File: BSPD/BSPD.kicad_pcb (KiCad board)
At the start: 2 copper layers, 26 parts, among them J1 440054-2, J2 440054-2, U1 LM339DR, U2 R-78E5.0-0.5, U3 SN74LVC1G08DBVR, U4 SN74LVC3G14DCUR, U5 NE555DR, U6 SN74LVC1G08DBVR, U8 SN74AC32DR

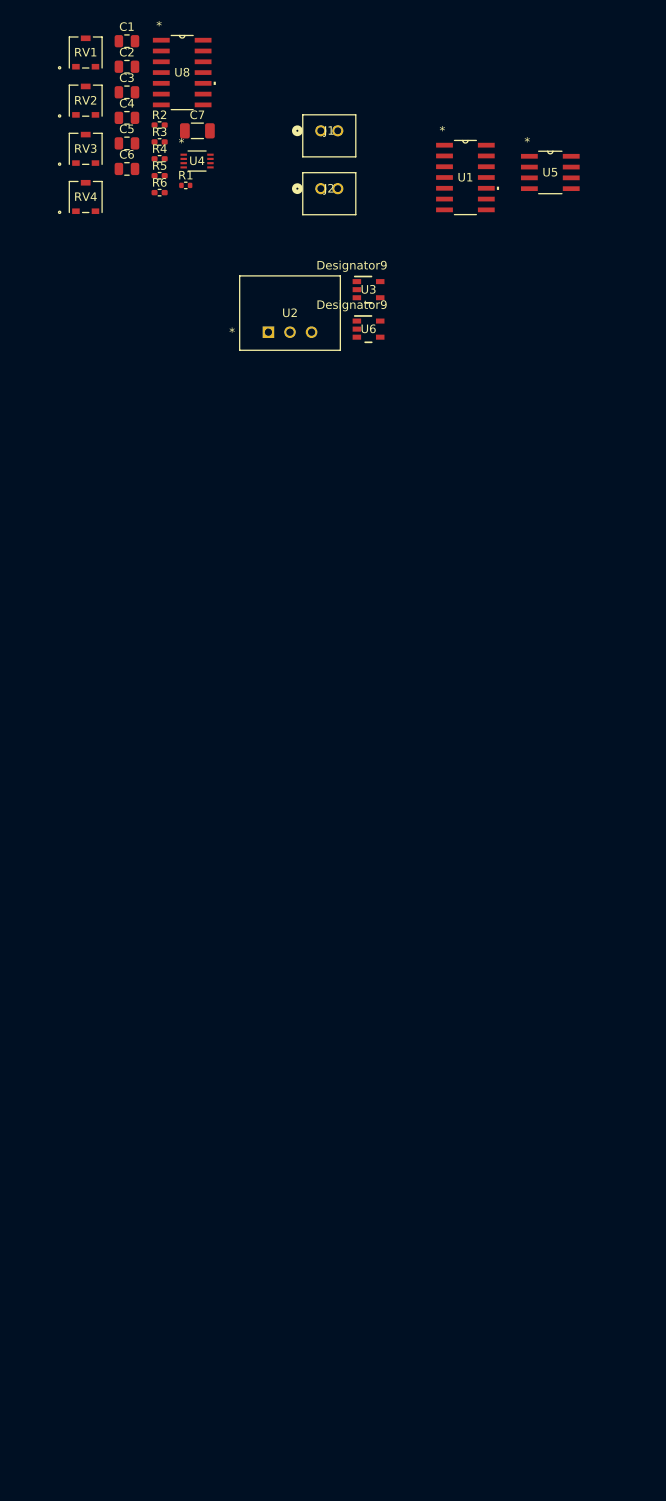
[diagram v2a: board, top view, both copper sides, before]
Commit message: Connector changes, layout, edge cuts, constraints. Need advice on output PMOS
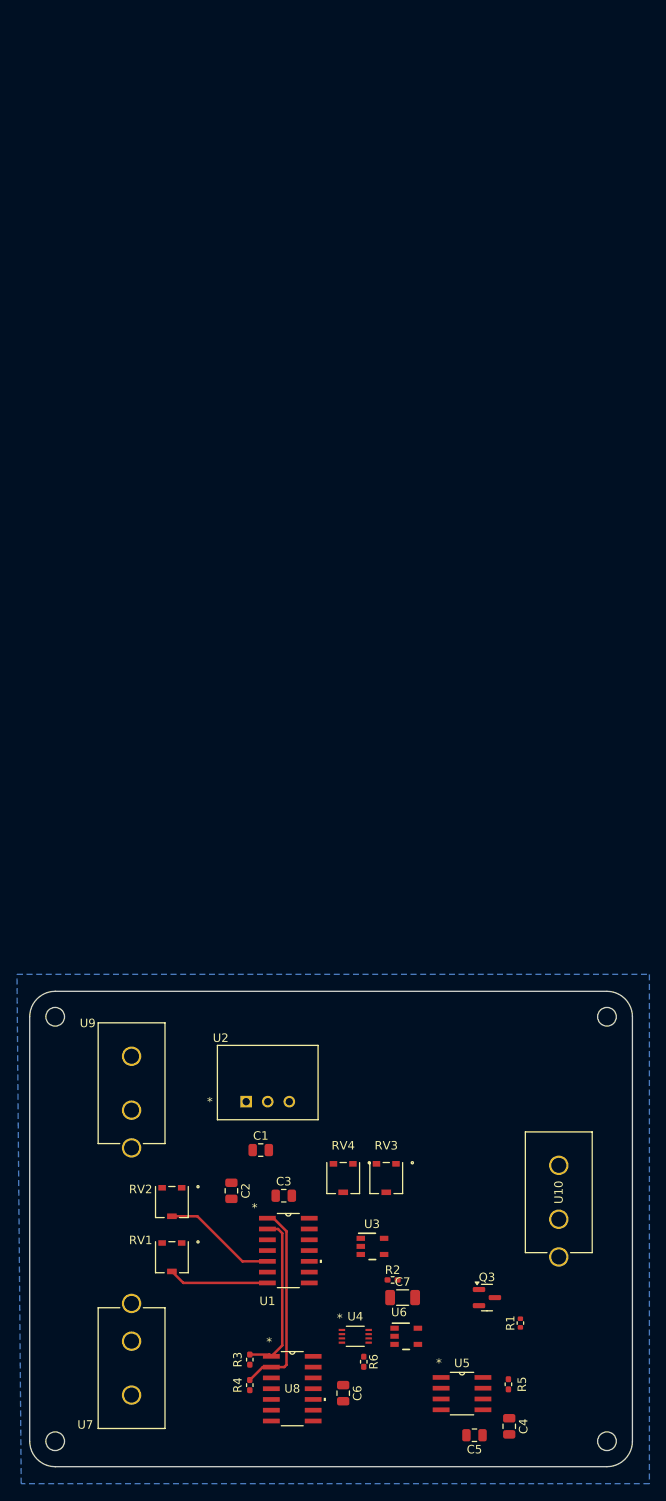
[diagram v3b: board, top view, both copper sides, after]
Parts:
- removed J1, J2: 440054-2, 440054_2:CONN2_440054-2_TYC
- added H1: MountingHole, MountingHole:MountingHole_2.2mm_M2, F.Cu at (117.5, 72.5)
- added H2: MountingHole, MountingHole:MountingHole_2.2mm_M2, F.Cu at (117.5, 122.5)
- added H3: MountingHole, MountingHole:MountingHole_2.2mm_M2, F.Cu at (182.5, 122.5)
- added H4: MountingHole, MountingHole:MountingHole_2.2mm_M2, F.Cu at (182.5, 72.5)
- added Q3: PMOS, Package_TO_SOT_SMD:SOT-23, F.Cu at (168.4, 105.6)
- added U10: 641964-1, 641964-1:641964-1_TYC, F.Cu at (176.8, 96.3)
- added U7: 641964-1, 641964-1:641964-1_TYC, F.Cu at (126.5, 110.7)
- added U9: 641964-1, 641964-1:641964-1_TYC, F.Cu at (126.5, 83.5)
- U8: footprint LM339DR:D14 -> SN74AC32DR:D14
- moved C4 160.6 mm to (171.0, 120.7), turned to -90 degrees
- moved C5 157.6 mm to (166.9, 121.8), turned to 180 degrees
- moved U8 155.6 mm to (145.4, 116.3)
- moved R5 148.2 mm to (170.9, 115.8), turned to 90 degrees
- moved C6 146.4 mm to (151.4, 116.8), turned to -90 degrees
- moved R4 144.8 mm to (140.4, 115.9), turned to -90 degrees
- moved U5 144.2 mm to (165.4, 116.9)
- moved R3 143.8 mm to (140.4, 112.9), turned to -90 degrees
- moved RV1 142.3 mm to (131.2, 100.8), turned to 180 degrees
- moved R6 139.8 mm to (153.9, 113.1), turned to -90 degrees
- moved U4 139.7 mm to (152.9, 110.1)
- moved R1 139.7 mm to (172.3, 108.6), turned to 90 degrees
- moved C7 139.6 mm to (158.4, 105.6)
- moved R2 138.8 mm to (157.2, 103.5)
- moved C2 133.0 mm to (138.3, 93.0), turned to -90 degrees
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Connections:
- C2 pad 1: Net-(U2-+VOUT) -> +5V
- C3 pad 1: Net-(U1-VCC) -> +5V
- RV1 pad 1: Net-(RV1-Pad1) -> +5V
- RV2 pad 1: Net-(RV2-Pad1) -> +5V
- RV3 pad 1: Net-(RV3-Pad1) -> +5V
- RV4 pad 1: Net-(RV4-Pad1) -> +5V
- U1 pad 3: Net-(U1-VCC) -> +5V
- U2 pad 3: Net-(U2-+VOUT) -> +5V
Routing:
- net 1OUT: track 0.00 -> 23.7 mm
- net 2OUT: track 0.00 -> 19.6 mm
- net THRESH_THROTTLE: track 0.00 -> 13.4 mm
- net THRESH_BSE: track 0.00 -> 11.8 mm
- added copper zone on B.Cu, net (none)
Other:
- board outline added: 71 x 56 mm

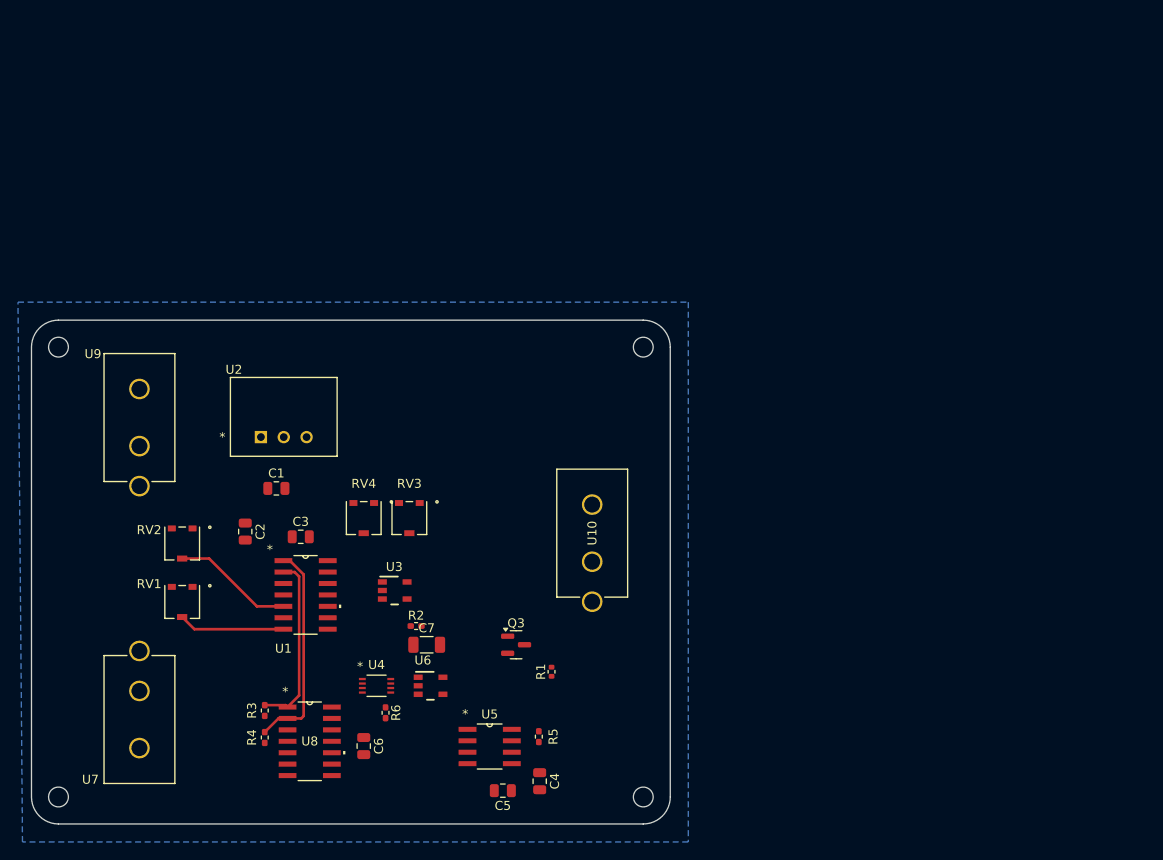
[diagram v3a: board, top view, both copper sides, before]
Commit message: Bypass caps bspd
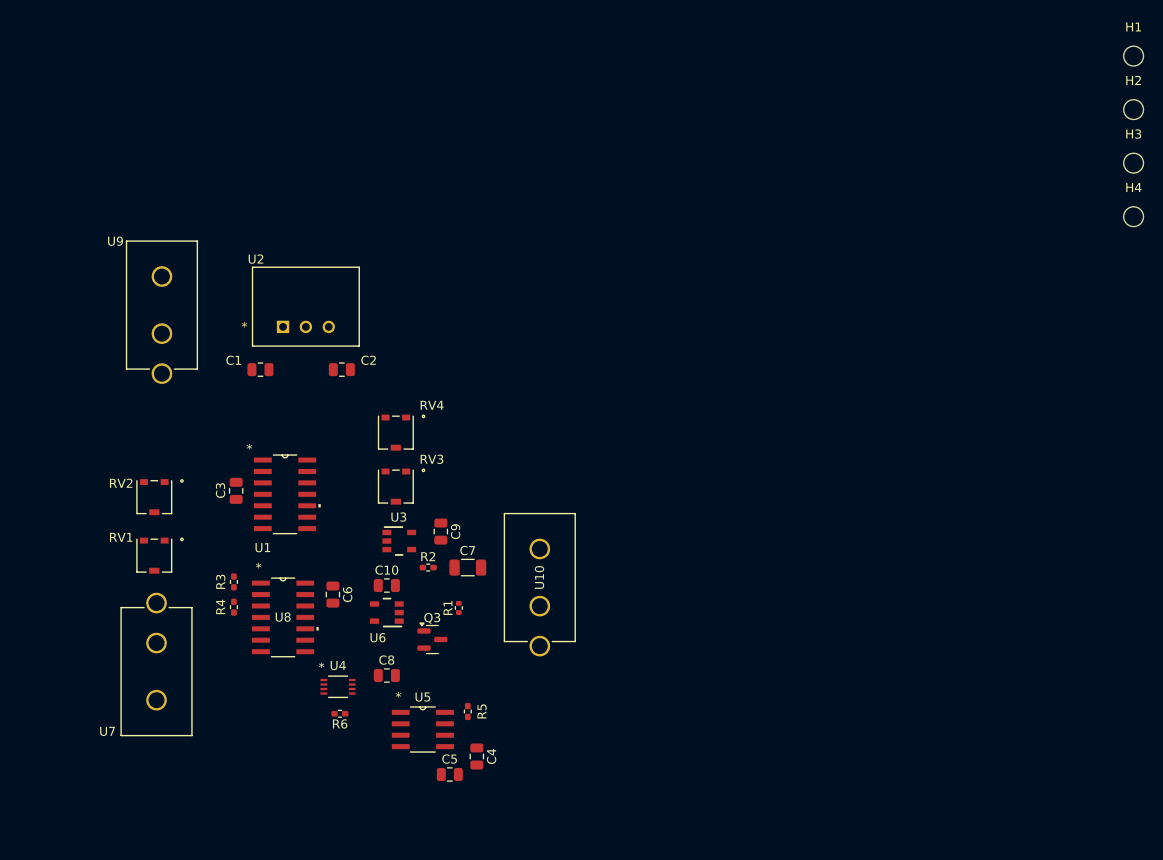
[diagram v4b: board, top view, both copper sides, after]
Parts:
- added C10: 0.1uF, Capacitor_SMD:C_0805_2012Metric, F.Cu at (154.0, 99.0)
- added C8: 0.1uF, Capacitor_SMD:C_0805_2012Metric, F.Cu at (154.0, 109.0)
- added C9: 0.1uF, Capacitor_SMD:C_0805_2012Metric, F.Cu at (160.0, 93.0)
- moved H2 141.8 mm to (237.0, 46.1)
- moved H1 123.8 mm to (237.0, 40.1)
- moved H3 89.1 mm to (237.0, 52.0)
- moved H4 56.4 mm to (237.0, 58.0)
- moved C2 21.0 mm to (149.0, 75.0), turned to 180 degrees
- moved C6 17.2 mm to (148.0, 100.0)
- moved R4 14.9 mm to (137.0, 101.4)
- moved R3 14.7 mm to (137.0, 98.6)
- moved U8 14.1 mm to (142.5, 102.5)
- moved C1 13.3 mm to (139.9, 75.0)
- moved U9 12.7 mm to (129.0, 71.0)
- moved R1 12.5 mm to (162.0, 101.5)
- moved U2 12.5 mm to (142.5, 70.2)
- moved U1 11.4 mm to (142.7, 88.9)
- moved RV4 10.1 mm to (155.0, 82.0)
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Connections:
- C6 pad 1: Net-(U8-4A) -> +5V
- R5 pad 2: Net-(U5-VCC) -> +5V
- U3 pad 5: Net-(U3-V+) -> +5V
- U4 pad 2: Net-(U4-3Y) -> +5V
- U4 pad 8: Net-(U4-VCC) -> +5V
- U5 pad 4: Net-(U5-RESET) -> +5V
- U5 pad 8: Net-(U5-VCC) -> +5V
- U6 pad 5: Net-(U6-V+) -> +5V
- U8 pad 12: Net-(U8-4A) -> +5V
- U8 pad 13: Net-(U8-4A) -> +5V
- U8 pad 14: Net-(U8-4A) -> +5V
- U8 pad 4: Net-(U8-2A) -> +5V
- U8 pad 5: Net-(U8-2A) -> +5V
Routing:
- net 1OUT: track 23.7 -> 0.00 mm
- net 2OUT: track 19.6 -> 0.00 mm
- net THRESH_THROTTLE: track 13.4 -> 0.00 mm
- net THRESH_BSE: track 11.8 -> 0.00 mm
- removed copper zone on B.Cu, net (none)
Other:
- board outline removed

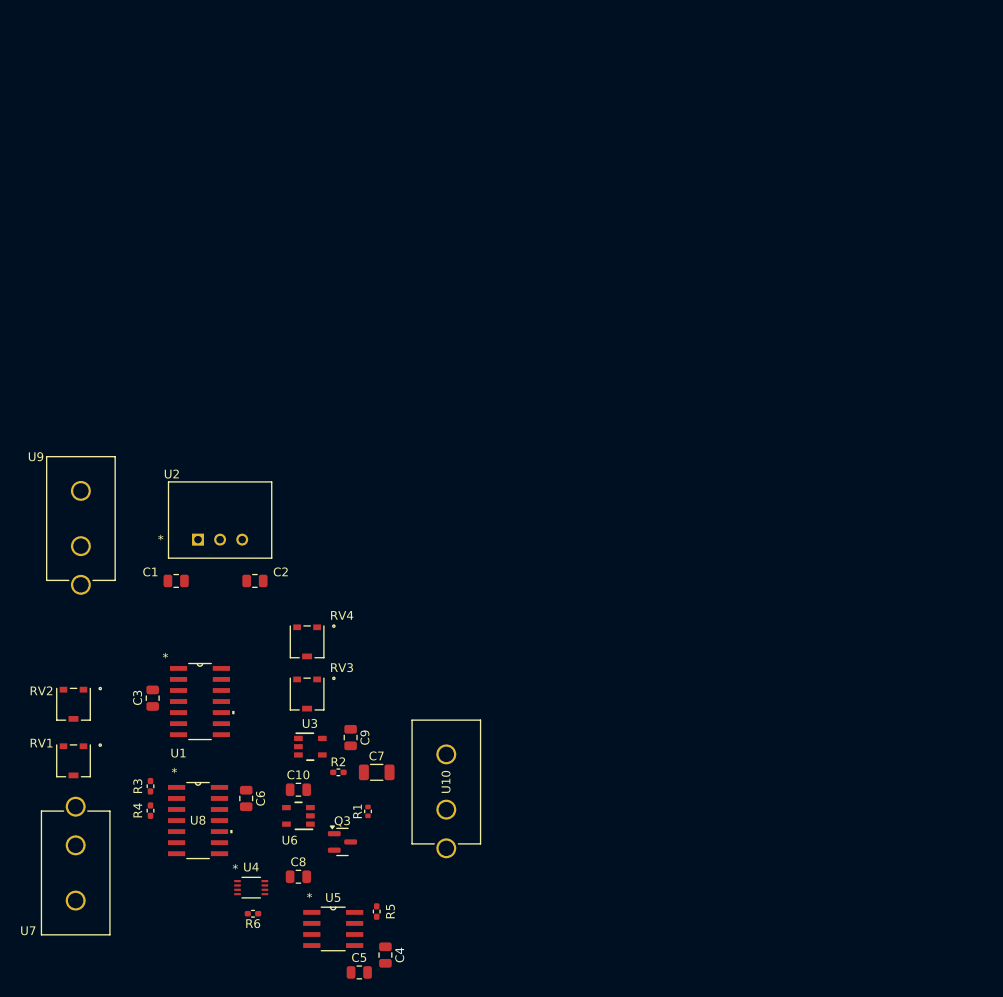
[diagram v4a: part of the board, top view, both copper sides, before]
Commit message: Redone logic for BSPD.
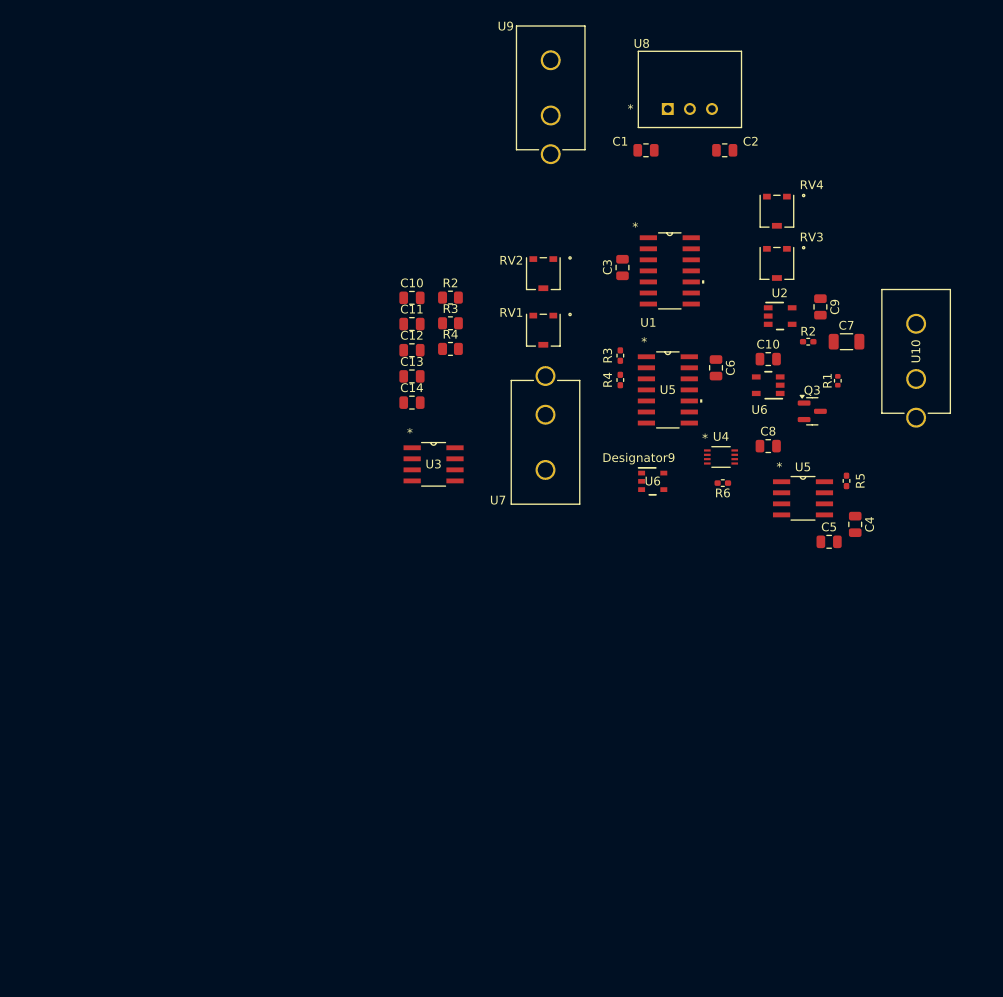
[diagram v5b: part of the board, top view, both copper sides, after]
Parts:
- added C10: 10uF, Capacitor_SMD:C_0805_2012Metric, F.Cu at (167.1, 42.5)
- added C11: 0.01uF, Capacitor_SMD:C_0805_2012Metric, F.Cu at (167.1, 45.5)
- added C12: 0.1uF, Capacitor_SMD:C_0805_2012Metric, F.Cu at (167.1, 48.5)
- added C13: 0.1uF, Capacitor_SMD:C_0805_2012Metric, F.Cu at (167.1, 51.5)
- added C14: 0.1uF, Capacitor_SMD:C_0805_2012Metric, F.Cu at (167.1, 54.5)
- added R2: 10K, Resistor_SMD:R_0805_2012Metric, F.Cu at (171.5, 42.4)
- added R3: 10K, Resistor_SMD:R_0805_2012Metric, F.Cu at (171.5, 45.4)
- added R4: 10K, Resistor_SMD:R_0805_2012Metric, F.Cu at (171.5, 48.3)
- added U3: NE555DR, NE555DR:D8, F.Cu at (169.5, 61.6)
- added U6: SN74LVC1G08DBVR, SN74LVC1G08DBVR:DBV0005A_L, F.Cu at (194.7, 63.6)
- R1: value R_US -> 10K
- moved C1 73.3 mm to (193.9, 25.5)
- moved C10 73.3 mm to (208.0, 49.5)
- moved C2 73.3 mm to (203.0, 25.5)
- moved C3 73.3 mm to (191.2, 39.0)
- moved C4 73.3 mm to (218.0, 68.5)
- moved C5 73.3 mm to (215.0, 70.5)
- moved C6 73.3 mm to (202.0, 50.5)
- moved C7 73.3 mm to (217.0, 47.5)
- moved C8 73.3 mm to (208.0, 59.5)
- moved C9 73.3 mm to (214.0, 43.5)
- moved Q3 73.3 mm to (213.1, 55.5)
- moved R1 73.3 mm to (216.0, 52.0)
- moved R2 73.3 mm to (212.6, 47.5)
- moved R3 73.3 mm to (191.0, 49.1)
- moved R4 73.3 mm to (191.0, 51.9)
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- renumbered U3 to U2, U8 to U5, U2 to U8
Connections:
- Q3 pad 2: BSPD_OUT -> Net-(Q3-G)
- U1 pad 13: Net-(U1-OUT4) -> 4OUT
- U1 pad 14: Net-(U1-OUT3) -> 3OUT
- U1 pad 4: THROTTLE_IN -> THRESH_THROTTLE
- U1 pad 5: THRESH_THROTTLE -> THROTTLE_IN
- U1 pad 6: BSE_IN -> THRESH_BSE
- U1 pad 7: THRESH_BSE -> BSE_IN
- U2 pad 1: Net-(U1-OUT3) -> 1OUT
- U2 pad 2: Net-(U1-OUT4) -> 2OUT
- U2 pad 4: Net-(U3-Y) -> Net-(U2-Y)
- U4 pad 1: Net-(U4-1A) -> Net-(U3-OUT)
- U4 pad 5: Net-(U4-2Y) -> +5V
- U4 pad 6: Net-(U4-3A) -> GND
- U4 pad 7: 1Y -> Net-(U4-1Y)
- U5 pad 1: 2OUT -> Net-(U4-1Y)
- U5 pad 10: Net-(U8-3B) -> +5V
- U5 pad 11: unconnected-(U8-4Y-Pad11) -> Net-(U5-4Y)
- U5 pad 12: +5V -> 4OUT
- U5 pad 13: +5V -> 3OUT
- U5 pad 2: 1OUT -> Net-(U2-Y)
- U5 pad 3: Net-(U4-1A) -> Net-(U5-1Y)
- U5 pad 8: BSPD_OUT -> unconnected-(U5-3Y-Pad8)
- U5 pad 9: Net-(U6-Y) -> +5V

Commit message: Layout
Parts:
- removed the C10 at (208.0, 49.5)
- removed the C10 at (167.1, 42.5)
- removed C4: 10uF, Capacitor_SMD:C_0805_2012Metric
- removed C5: 0.01uF, Capacitor_SMD:C_0805_2012Metric
- removed C6, C8: 0.1uF, Capacitor_SMD:C_0805_2012Metric
- removed C7: 100uF, Capacitor_SMD:C_1206_3216Metric
- removed the R2 at (212.6, 47.5)
- removed the R2 at (171.5, 42.4)
- removed the R3 at (171.5, 45.4)
- removed the R3 at (191.0, 49.1)
- removed the R4 at (191.0, 51.9)
- removed the R4 at (171.5, 48.3)
- removed R5, R6: 10K, Resistor_SMD:R_0402_1005Metric_Pad0.72x0.64mm_HandSolder
- removed the U5 at (196.5, 53.0)
- removed the U5 at (212.0, 65.5)
- removed the U6 at (208.0, 52.5)
- removed the U6 at (194.7, 63.6)
- added C10: 10uF, Capacitor_SMD:C_0805_2012Metric, F.Cu at (160.5, 136.0)
- added R2: 10K, Resistor_SMD:R_0805_2012Metric, F.Cu at (160.5, 132.1)
- added R3: 10K, Resistor_SMD:R_0805_2012Metric, F.Cu at (154.5, 127.2)
- added R4: 10K, Resistor_SMD:R_0805_2012Metric, F.Cu at (164.1, 128.0)
- added U5: SN74AC32DR, LM339DR:D14, F.Cu at (164.5, 112.6)
- added U6: SN74LVC1G08DBVR, SN74LVC1G08DBVR:DBV0005A_L, F.Cu at (171.3, 116.9)
- moved H2 150.5 mm to (121.0, 142.0)
- moved H1 127.1 mm to (121.0, 92.0)
- moved U2 111.9 mm to (140.0, 132.4)
- moved C9 111.0 mm to (144.9, 130.4), turned to 0 degrees
- moved RV4 103.4 mm to (151.8, 118.7)
- moved H3 101.0 mm to (191.0, 142.0)
- moved U8 96.4 mm to (146.9, 103.5)
- moved C11 94.1 mm to (154.0, 138.6), turned to 180 degrees
- moved U1 94.0 mm to (141.2, 115.3)
- moved RV3 93.4 mm to (151.8, 112.4)
- moved C2 92.8 mm to (157.0, 106.0), turned to -90 degrees
- moved U9 92.3 mm to (131.0, 97.7), turned to -90 degrees
- moved C1 91.0 mm to (141.0, 99.5), turned to -90 degrees
- moved RV2 90.6 mm to (129.8, 113.7)
- moved RV1 90.2 mm to (129.8, 119.7)
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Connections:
- U1 pad 10: HARD_BREAK -> 10%_THROTTLE
- U1 pad 11: BSE_IN -> THROTTLE_IN
- U1 pad 8: 10%_THROTTLE -> HARD_BREAK
- U1 pad 9: THROTTLE_IN -> BSE_IN
- U4 pad 6: GND -> Net-(U4-3A)
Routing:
- net +5V: track 0.00 -> 203.9 mm, vias 0 -> 8
- net Net-(U2-Y): track 0.00 -> 39.7 mm
- net GND: track 0.00 -> 30.5 mm, vias 0 -> 21
- net 3OUT: track 0.00 -> 28.4 mm, vias 0 -> 2
- net 4OUT: track 0.00 -> 28.4 mm, vias 0 -> 2
- net BSE_IN: track 0.00 -> 26.5 mm
- net 2OUT: track 0.00 -> 24.8 mm, vias 0 -> 2
- net THROTTLE_IN: track 0.00 -> 23.7 mm, vias 0 -> 2
- net 1OUT: track 0.00 -> 23.0 mm, vias 0 -> 2
- net Net-(U4-1Y): track 0.00 -> 19.8 mm, vias 0 -> 2
- net Net-(U5-1Y): track 0.00 -> 16.4 mm, vias 0 -> 2
- net Net-(U3-OUT): track 0.00 -> 12.5 mm, vias 0 -> 2
- net BSPD_TO_FAULT: track 0.00 -> 12.5 mm
- net THRESH_BSE: track 0.00 -> 10.3 mm
- net 10%_THROTTLE: track 0.00 -> 9.86 mm, vias 0 -> 2
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- added copper zone on F.Cu, net +12V
- added copper zone on F.Cu, net +5V
- added copper zone on B.Cu, net GND
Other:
- board outline added: 76 x 56 mm
- board text added: "1)THROTTLE 2)B.S.E"
- board text added: "12V (LVS)"
- board text added: "12V(LVS)-5V"
- board text added: "BSE THRESH"
- board text added: "THROTTLE THRESH"
